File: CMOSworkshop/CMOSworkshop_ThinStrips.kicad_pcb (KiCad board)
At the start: 2 copper layers, 160.5 x 65.6 mm, 68 parts, among them J1 JACK_STEREO, P1 CONN_01X03, P10 CONN_01X02, P11 CONN_01X03, P12 CONN_01X02, P13 CONN_01X03, P14 CONN_01X02, P15 CONN_01X03, P16 CONN_01X02, P17 CONN_01X02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

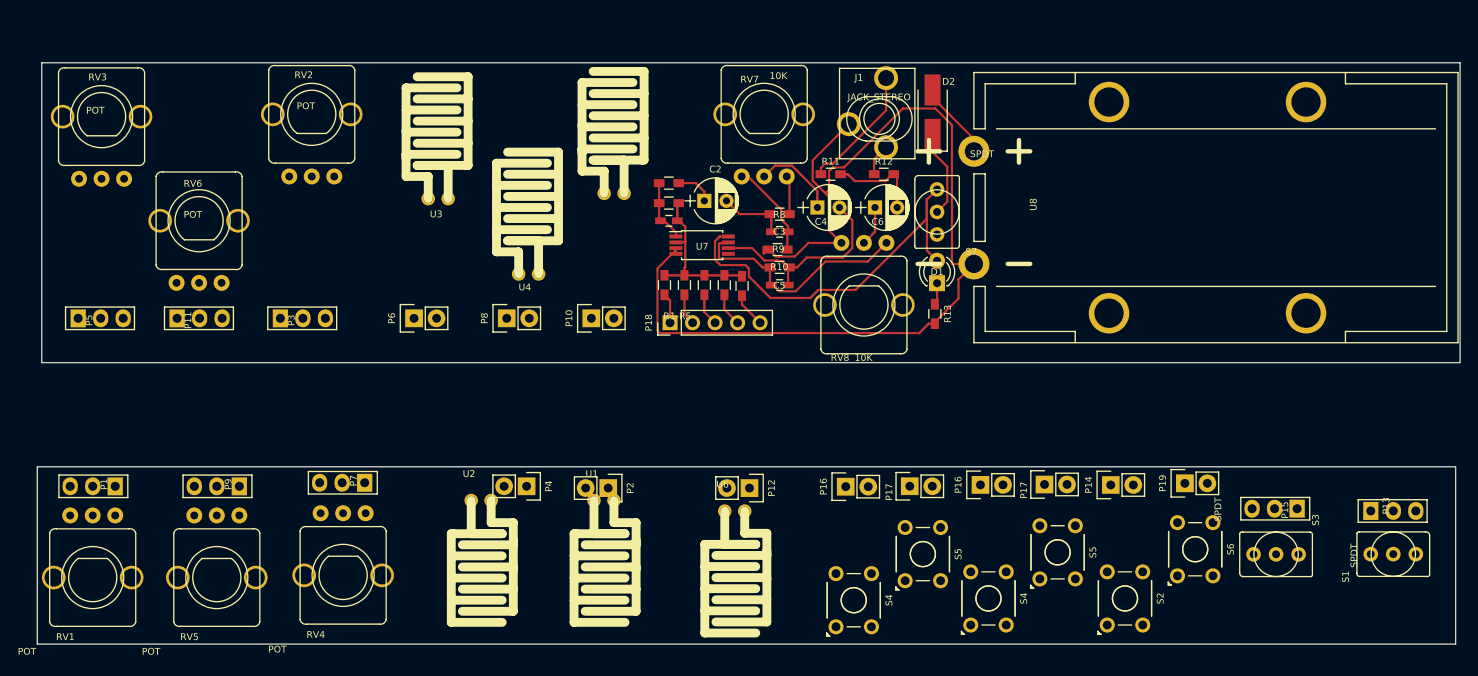
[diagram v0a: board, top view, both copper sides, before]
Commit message: changed touchpads to copper and adjusted for 2.54mm spacing
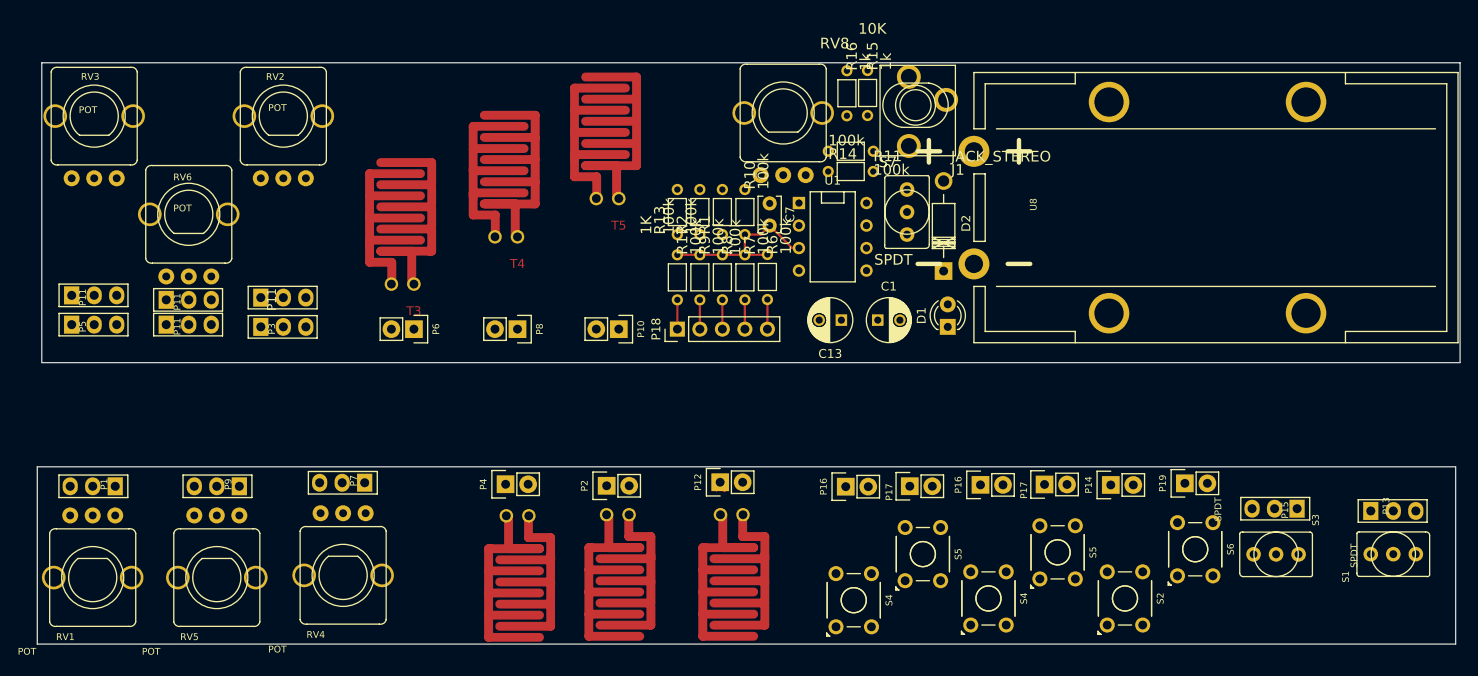
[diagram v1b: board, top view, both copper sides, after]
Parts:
- removed C2, C4: 1uF, DRCs parts:Capacitor_TH_Electrolytic
- removed C3: .1uF, Capacitors_SMD:C_0603_HandSoldering
- removed C5: 47pF, Capacitors_SMD:C_0603_HandSoldering
- removed C6: 10uF, DRCs parts:Capacitor_TH_Electrolytic
- removed R1-R5, R3, R4: 10k, Resistors_SMD:R_0603_HandSoldering
- removed R12: 100k, Resistors_SMD:R_0603_HandSoldering
- removed RV7: 10K, 4ms-footprints:POT-9MM-ALPHA
- removed U2, U3, U4, U5, U6: Touchpad, Connect:touchpad3
- removed U7: TL082, Housings_SSOP:TSSOP-8_4.4x3mm_Pitch0.65mm
- added C13: 100uF, Capacitors_ThroughHole:C_Radial_D5_L6_P2.5, F.Cu at (190.2, 108.2)
- added C7: 47pF, Capacitors_THT:C_Rect_L4.0mm_W2.5mm_P2.50mm, F.Cu at (182.1, 95.0)
- added P11: CONN_01X03, 4ms-footprints:Pin_Header_Straight_1x03, F.Cu at (103.4, 105.4)
- added P11: CONN_01X03, 4ms-footprints:Pin_Header_Straight_1x03, F.Cu at (114.0, 105.9)
- added P11: CONN_01X03, 4ms-footprints:Pin_Header_Straight_1x03, F.Cu at (124.7, 105.7)
- added R14: 100k, 4ms-footprints:R-TH, F.Cu at (191.3, 91.4)
- added R15: 1k, 4ms-footprints:R-TH, F.Cu at (193.2, 82.6)
- added R16: 1k, 4ms-footprints:R-TH, F.Cu at (190.8, 82.6)
- added R17: 100k, 4ms-footprints:R-TH, F.Cu at (171.7, 103.4)
- added T1: Touchpad, DRCs parts:touchpadCopper, F.Cu at (163.7, 127.6)
- added T2: Touchpad, DRCs parts:touchpadCopper, F.Cu at (152.4, 127.7)
- added T3: Touchpad, DRCs parts:touchpadCopper, F.Cu at (142.0, 106.7)
- added T4: Touchpad, DRCs parts:touchpadCopper, F.Cu at (153.7, 101.3)
- added T5: Touchpad, DRCs parts:touchpadCopper, F.Cu at (165.1, 97.0)
- added T6: Touchpad, DRCs parts:touchpadCopper, F.Cu at (176.6, 127.6)
- C1: value 27pF -> 100uF; footprint Capacitors_SMD:C_0603_HandSoldering -> Capacitors_ThroughHole:C_Radial_D5_L6_P2.5
- D2: footprint Diodes_SMD:D_SMA_Handsoldering -> Diodes_ThroughHole:Diode_DO-41_SOD81_Horizontal_RM10
- R1, R10, R2, R6, R7: value 10k -> 100k; footprint Resistors_SMD:R_0603_HandSoldering -> 4ms-footprints:R-TH
- R11, R13: footprint Resistors_SMD:R_0603_HandSoldering -> 4ms-footprints:R-TH
- R8: value 10K -> 100k; footprint Resistors_SMD:R_0603_HandSoldering -> 4ms-footprints:R-TH
- R9: value 2.2k -> 100k; footprint Resistors_SMD:R_0603_HandSoldering -> 4ms-footprints:R-TH
- U1: value Touchpad -> TL082; footprint Connect:touchpad3 -> Sockets_DIP:DIP-8__300
- moved U1 38.5 mm to (189.2, 98.8), turned to 270 degrees
- moved R13 31.2 mm to (171.7, 96.0), turned to 90 degrees
- moved C1 26.1 mm to (194.3, 108.2)
- moved RV8 23.5 mm to (183.6, 84.8), turned to 180 degrees
- moved D2 18.0 mm to (201.7, 102.7)
- moved R6 13.9 mm to (181.9, 103.3), turned to 270 degrees
- moved R7 13.7 mm to (179.3, 103.4), turned to 270 degrees
- moved R8 9.62 mm to (176.8, 103.4), turned to 270 degrees
- moved R9 9.30 mm to (174.2, 103.4), turned to 270 degrees
- moved R2 8.69 mm to (174.2, 96.0), turned to 90 degrees
- moved R1 8.63 mm to (176.8, 96.0), turned to 90 degrees
- moved R10 7.37 mm to (179.3, 96.0), turned to 270 degrees
- moved D1 5.07 mm to (202.2, 109.0)
- moved J1 4.35 mm to (198.6, 84.0), turned to 180 degrees
- moved R11 3.45 mm to (191.3, 89.2), turned to 180 degrees
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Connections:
- R1 pad 1: Net-(C1-Pad2) -> VCC
- R1 pad 2: MIX1 -> Net-(C1-Pad+)
- R10 pad 1: Net-(C5-Pad1) -> Net-(C7-Pad1)
- R10 pad 2: Net-(C4-Pad-) -> Net-(C7-Pad2)
- R11 pad 1: MIXOUTA -> Net-(R11-Pad1)
- R11 pad 2: Net-(C6-Pad-) -> Net-(R11-Pad2)
- R2 pad 1: Net-(C1-Pad2) -> GND
- R2 pad 2: MIX2 -> Net-(C1-Pad+)
- R6 pad 1: Net-(C1-Pad1) -> Net-(C7-Pad2)
- R6 pad 2: Net-(C1-Pad2) -> MIX1
- R7 pad 1: Net-(C2-Pad+) -> Net-(C7-Pad2)
- R7 pad 2: Net-(C1-Pad1) -> MIX2
- R8 pad 1: Net-(R8-Pad1) -> Net-(C7-Pad2)
- R8 pad 2: Net-(C2-Pad-) -> MIX3
- R9 pad 1: Net-(C3-Pad1) -> Net-(C7-Pad2)
- R9 pad 2: GND -> MIX4
- RV8 pad 1: Net-(C5-Pad1) -> Net-(C7-Pad1)
- RV8 pad 2: Net-(C6-Pad+) -> Net-(R11-Pad2)
- RV8 pad 3: GND -> Net-(C1-Pad+)
- U1 pad 1: Net-(P2-Pad2) -> Net-(C7-Pad1)
- U1 pad 2: Net-(P2-Pad1) -> Net-(C1-Pad+)
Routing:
- net GND: track 115.7 -> 0.00 mm
- net VCC: track 44.9 -> 0.00 mm
- net Net-(C5-Pad1): track 26.5 -> 0.00 mm
- net Net-(C4-Pad-): track 23.0 -> 0.00 mm
- net Net-(C7-Pad2): track 0.00 -> 20.0 mm
- net Net-(C1-Pad2): track 18.6 -> 0.00 mm
- net MIXOUTA: track 14.4 -> 0.00 mm
- net Net-(C3-Pad1): track 10.9 -> 0.00 mm
- net Net-(C6-Pad-): track 10.6 -> 0.00 mm
- net Net-(D2-Pad1): track 9.91 -> 0.00 mm
- net Net-(C4-Pad+): track 9.55 -> 0.00 mm
- net Net-(C2-Pad-): track 7.58 -> 0.00 mm
- net Net-(D2-Pad2): track 8.84 -> 1.40 mm
- net Net-(C1-Pad1): track 7.08 -> 0.00 mm
- net Net-(C6-Pad+): track 4.51 -> 0.00 mm
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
